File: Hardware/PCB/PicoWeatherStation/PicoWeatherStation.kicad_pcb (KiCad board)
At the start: 2 copper layers, 99.2 x 73 mm, 83 parts, among them J1 TOUCH_PANEL, J2 LCD_BL, Q1 AO3400A, SW1 SW_PICO_RST, SW2 SW_PICO_RST, SW3 SW_PICO_RST, SW4 SW_PICO_RST, SW5 SW_PICO_RST, SW6 SW_PICO_RST, SW7 SW_PICO_RST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

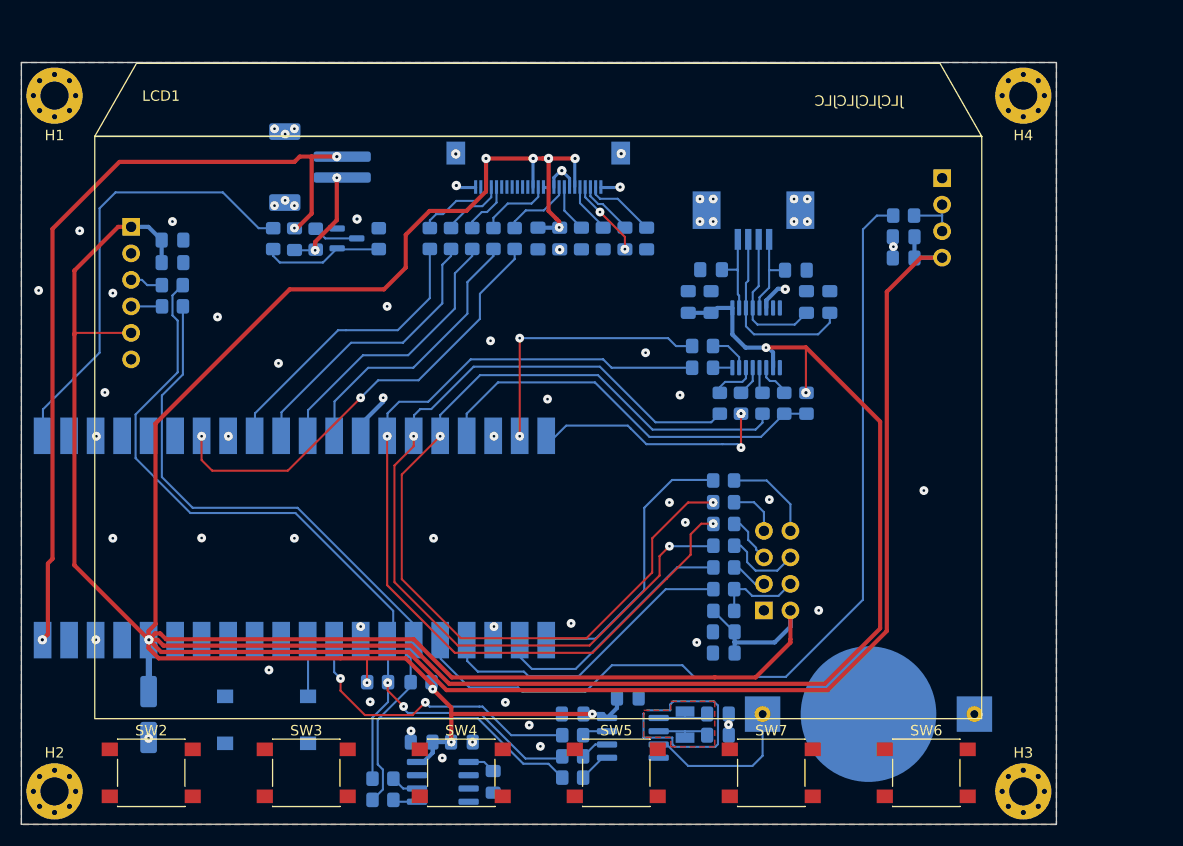
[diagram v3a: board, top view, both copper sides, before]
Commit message: PCB: wire-up the keyboard
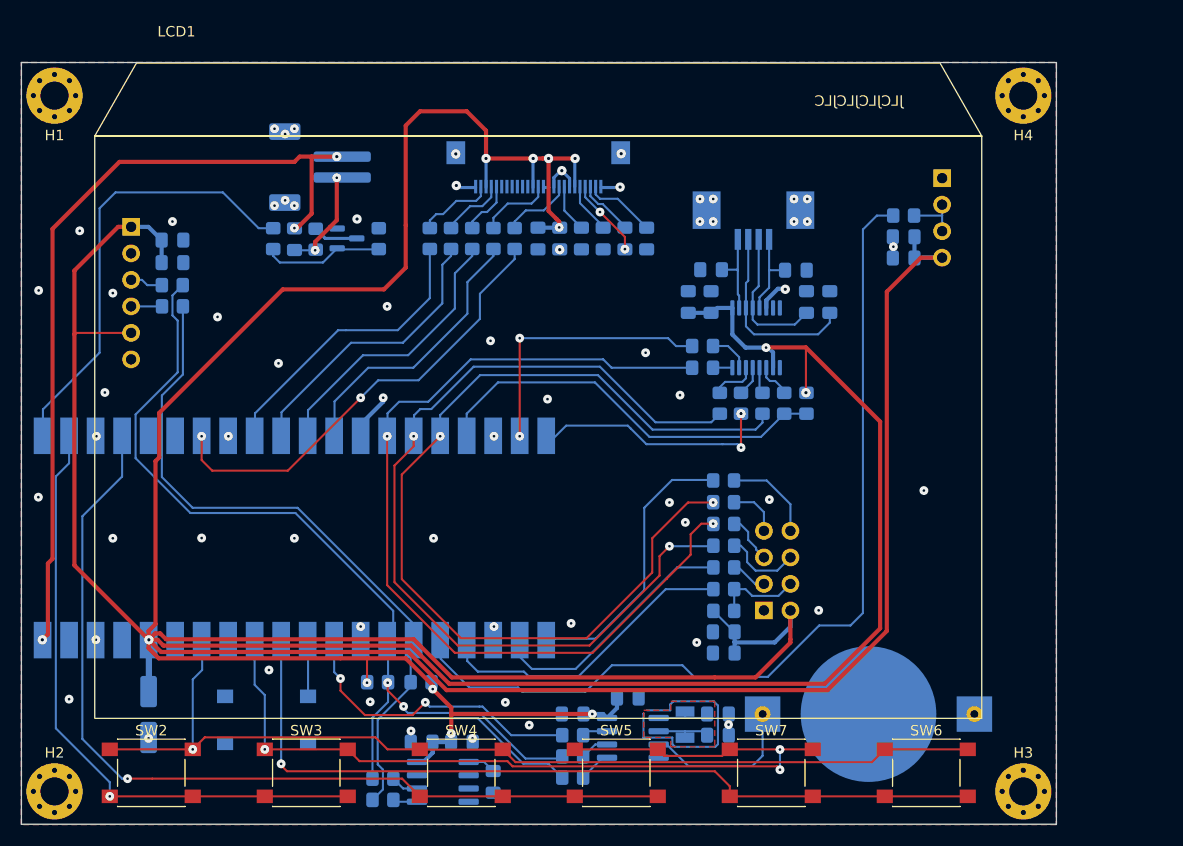
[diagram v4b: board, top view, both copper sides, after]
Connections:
- SW2 pad 1: unconnected-(SW2-Pad1) -> KBD_SCAN0
- SW2 pad 2: unconnected-(SW2-Pad2) -> KBD_DRV0
- SW3 pad 1: unconnected-(SW3-Pad1) -> KBD_SCAN1
- SW3 pad 2: unconnected-(SW3-Pad2) -> KBD_DRV0
- SW4 pad 1: unconnected-(SW4-Pad1) -> KBD_SCAN0
- SW4 pad 2: unconnected-(SW4-Pad2) -> KBD_DRV1
- SW5 pad 1: unconnected-(SW5-Pad1) -> KBD_SCAN1
- SW5 pad 2: unconnected-(SW5-Pad2) -> KBD_DRV1
- SW6 pad 1: unconnected-(SW6-Pad1) -> KBD_SCAN0
- SW6 pad 2: unconnected-(SW6-Pad2) -> KBD_DRV2
- SW7 pad 1: unconnected-(SW7-Pad1) -> KBD_SCAN1
- SW7 pad 2: unconnected-(SW7-Pad2) -> KBD_DRV2
- U1 pad 2: unconnected-(U1-Pad2) -> KBD_DRV0
- U1 pad 31: unconnected-(U1-Pad31) -> KBD_DRV2
- U1 pad 32: unconnected-(U1-Pad32) -> KBD_SCAN1
- U1 pad 34: unconnected-(U1-Pad34) -> KBD_SCAN0
- U1 pad 4: unconnected-(U1-Pad4) -> KBD_DRV1
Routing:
- net KBD_SCAN0: track 0.00 -> 96.0 mm, vias 0 -> 1
- net KBD_SCAN1: track 0.00 -> 87.2 mm, vias 0 -> 3
- net KBD_DRV1: track 0.00 -> 87.2 mm, vias 0 -> 1
- net KBD_DRV2: track 0.00 -> 80.5 mm, vias 0 -> 1
- net KBD_DRV0: track 0.00 -> 59.1 mm, vias 0 -> 1
- net VDD: track 542.2 -> 551.5 mm
- net ZR_OUT: track 88.0 -> 88.8 mm

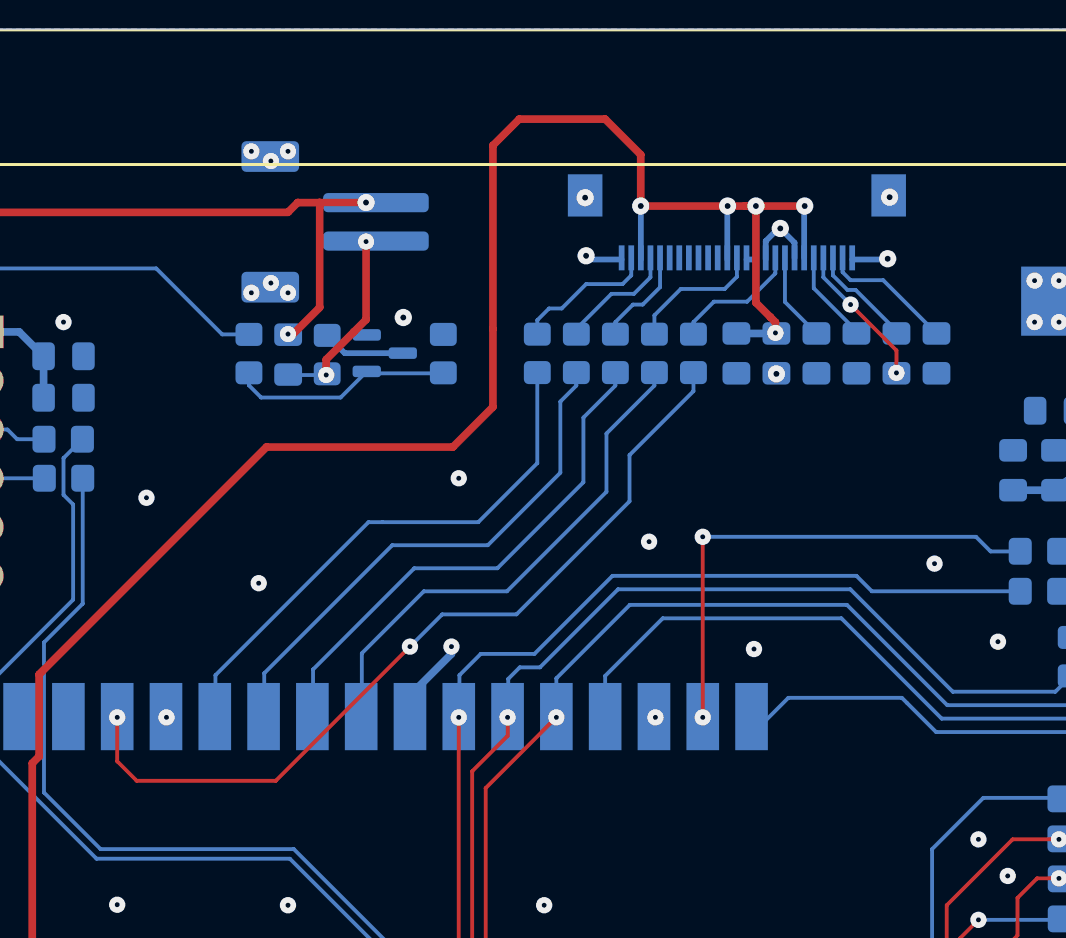
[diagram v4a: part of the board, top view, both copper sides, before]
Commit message: PCB: optimize high speed LCD signal tracks
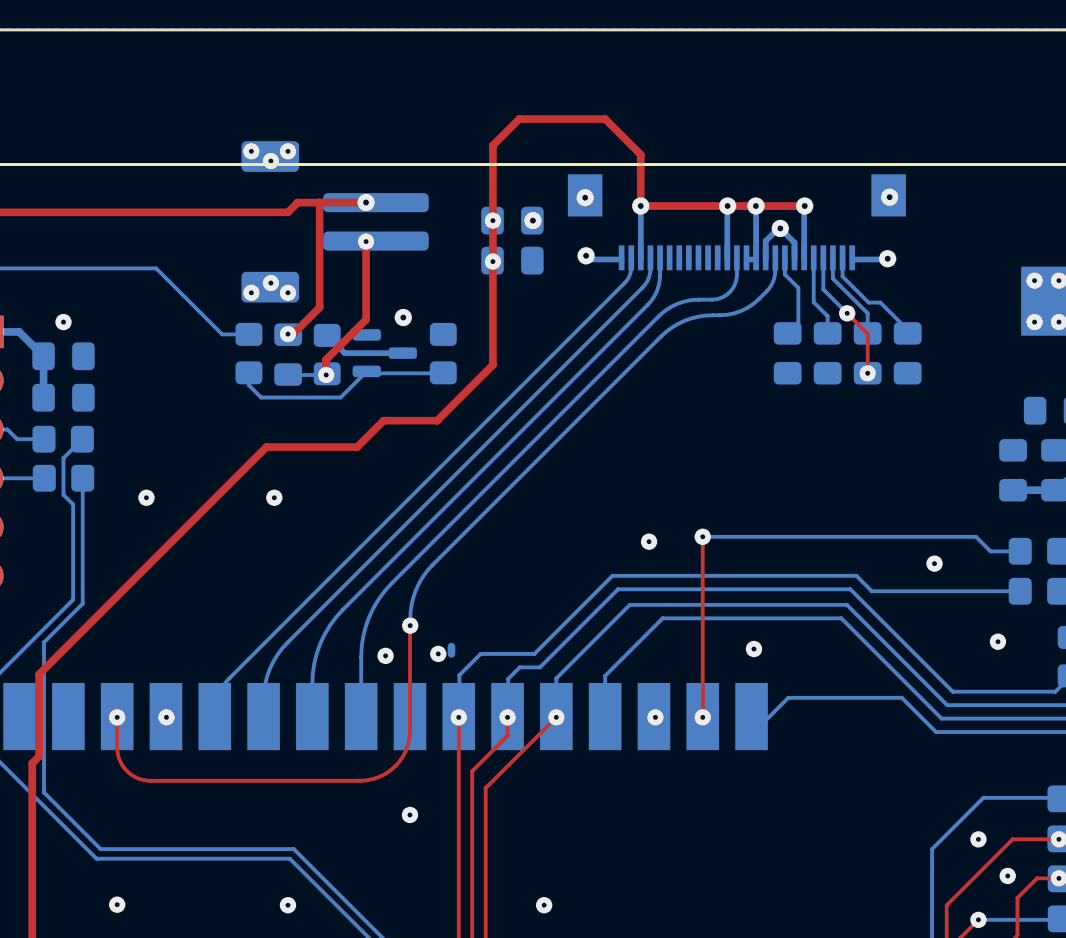
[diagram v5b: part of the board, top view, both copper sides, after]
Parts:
- removed R101, R102, R103, R104, R105: 270, Resistor_SMD:R_0805_2012Metric_Pad1.20x1.40mm_HandSolder
- moved C102 15.4 mm to (120.4, 49.3), turned to 0 degrees
- moved C101 12.6 mm to (120.4, 51.4), turned to 0 degrees
- moved C111 1.50 mm to (141.0, 56.2)
- moved C112 1.50 mm to (138.9, 56.2)
- moved C113 1.50 mm to (136.8, 56.2)
- moved C114 1.50 mm to (134.7, 56.2)
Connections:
- LCD1 pad 13: Net-(LCD1-Pad13) -> LCD_~{RST}
- LCD1 pad 21: Net-(LCD1-Pad21) -> LCD_D~{C}
- LCD1 pad 22: Net-(LCD1-Pad22) -> LCD_SDI
- LCD1 pad 24: Net-(LCD1-Pad24) -> LCD_SCK
- LCD1 pad 9: Net-(LCD1-Pad9) -> LCD_~{CS}
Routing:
- net VDD: track 551.5 -> 541.2 mm, vias 12 -> 13
- net LCD_~{CS}: track 43.5 -> 52.7 mm
- net Net-(LCD1-Pad24): track 7.48 -> 0.00 mm
- net Net-(LCD1-Pad13): track 7.08 -> 0.00 mm
- net Net-(LCD1-Pad9): track 6.74 -> 0.00 mm
- net Net-(LCD1-Pad22): track 6.24 -> 0.00 mm
- net LCD_~{RST}: track 27.7 -> 33.8 mm
- net Net-(LCD1-Pad21): track 5.22 -> 0.00 mm
- net LCD_SCK: track 29.1 -> 33.6 mm
- net LCD_SDI: track 28.5 -> 32.9 mm
- net LCD_D~{C}: track 27.9 -> 31.9 mm
- net GND: track 37.0 -> 34.0 mm, vias 63 -> 64
- net LCD_VG: track 6.94 -> 5.69 mm
- net LCD_XV0: track 5.54 -> 4.68 mm
- net LCD_VM: track 4.84 -> 4.23 mm
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
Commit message: PCB: do minor track optimization
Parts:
- moved C113 0.30 mm to (136.5, 56.2)
- moved C114 0.30 mm to (134.4, 56.2)
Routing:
- net VDD: track 541.2 -> 538.4 mm
- net GND: track 34.0 -> 33.6 mm, vias 64 -> 66
- net LCD_V0: vias 2 -> 0
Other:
- board text removed: "ZR_OUT"

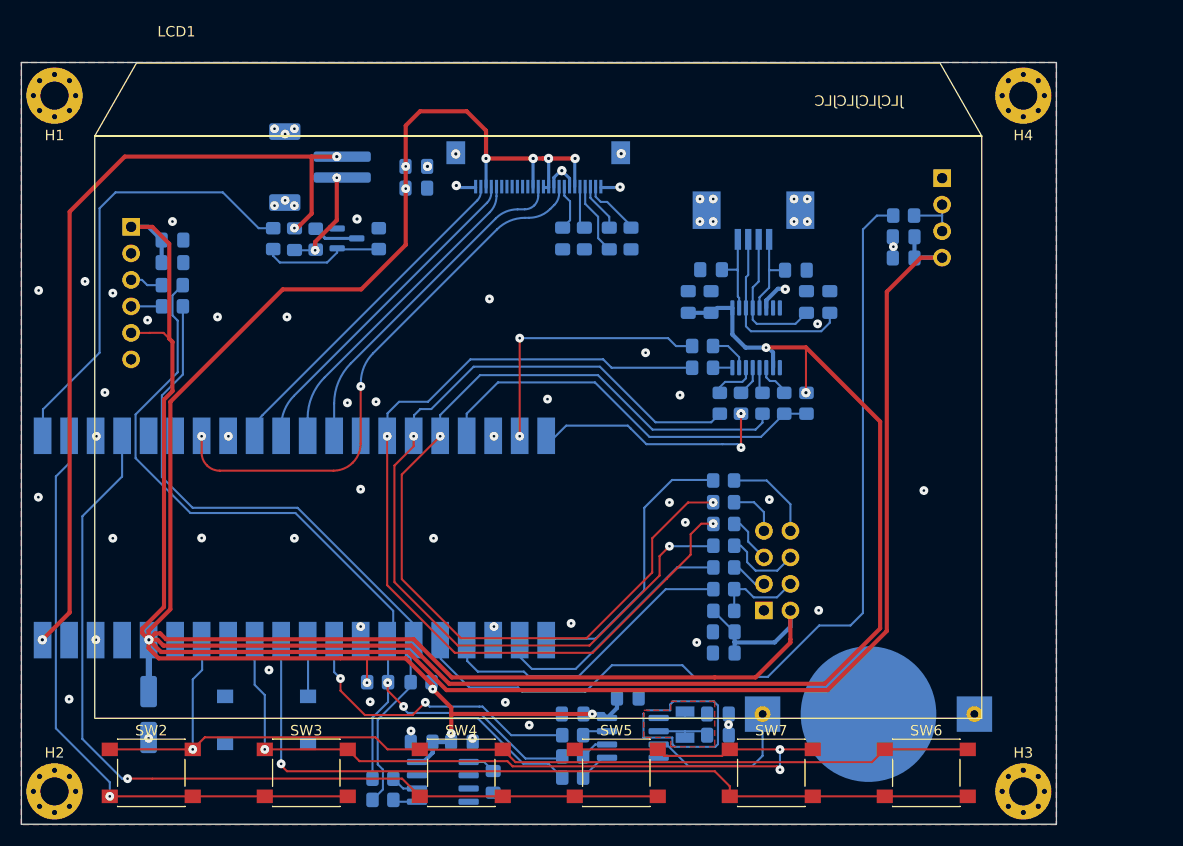
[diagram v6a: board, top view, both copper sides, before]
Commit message: PCB: optimize peripheral SPI signals
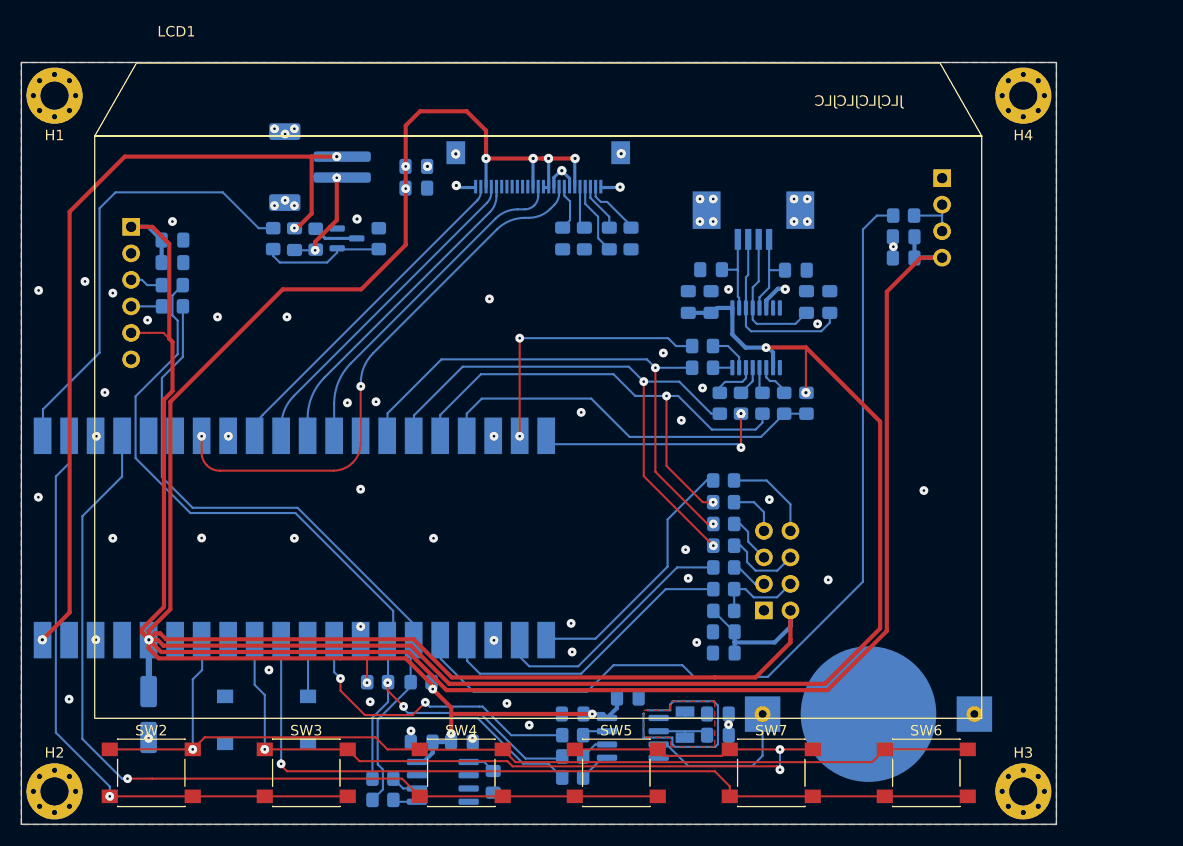
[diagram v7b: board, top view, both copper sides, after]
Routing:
- net SPI_PERI_MISO: track 93.4 -> 51.4 mm
- net SPI_PERI_SCK: track 89.2 -> 52.3 mm
- net SPI_PERI_MOSI: track 89.5 -> 54.5 mm
- net NRF_IRQ: track 29.2 -> 27.2 mm
- net ZR_OUT: track 88.8 -> 87.0 mm
- net TOUCH_BUSY: track 23.5 -> 22.1 mm
- net TOUCH_~{PENIRQ}: track 39.9 -> 38.6 mm
- net GND: vias 66 -> 69

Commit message: PCB: bigger footprint for the clock crystal
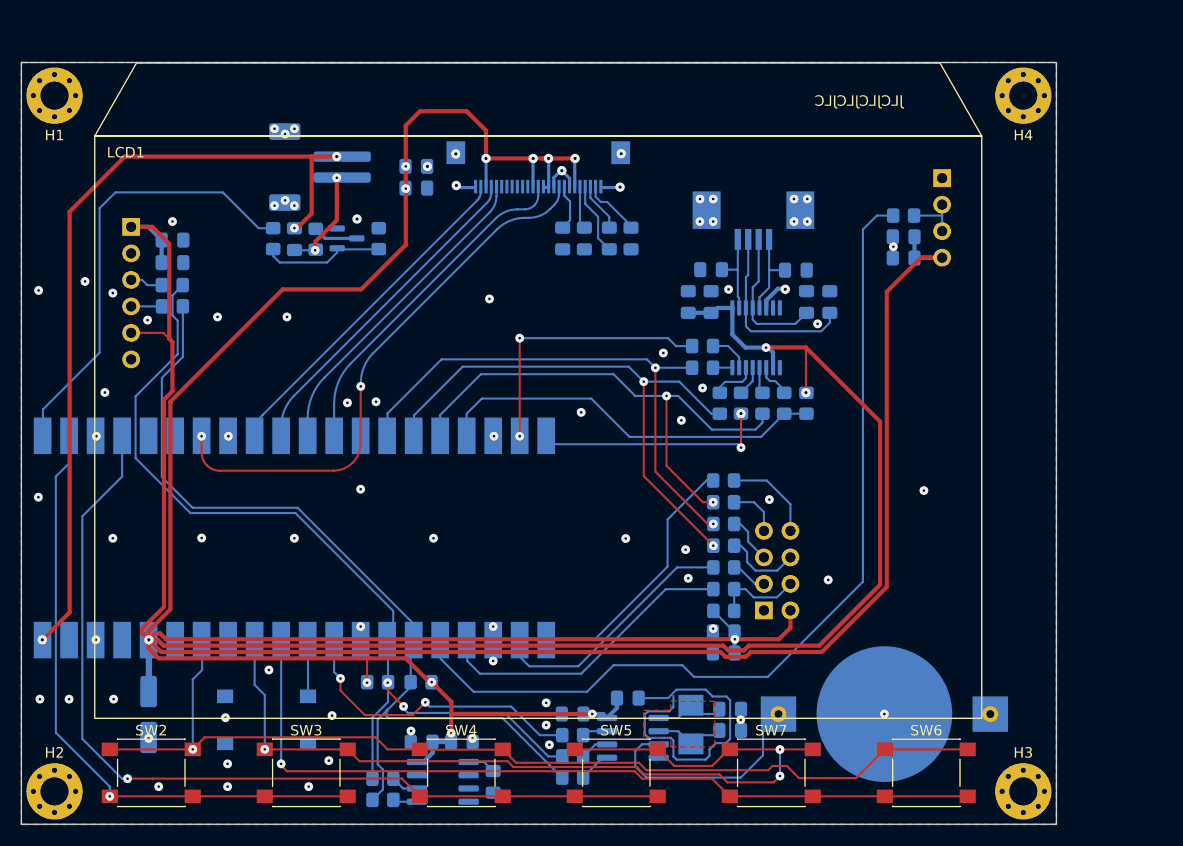
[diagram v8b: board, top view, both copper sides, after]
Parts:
- Y1: footprint Crystal:Crystal_SMD_3215-2Pin_3.2x1.5mm -> Crystal:Crystal_SMD_5032-2Pin_5.0x3.2mm
- moved BT1 1.52 mm to (165.2, 101.8)
- moved CX1 1.26 mm to (150.5, 101.3)
- moved CX2 1.26 mm to (150.5, 103.4)
- moved Y1 0.56 mm to (146.7, 102.8), turned to 90 degrees
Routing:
- net VDD: track 538.4 -> 517.5 mm, vias 13 -> 14
- net GND: track 33.6 -> 42.4 mm, vias 69 -> 79
- net Net-(BT1-Pad1): track 15.2 -> 23.3 mm
- net KBD_SCAN1: track 87.2 -> 89.4 mm
- net KBD_SCAN0: track 96.0 -> 97.6 mm
- net Net-(CX2-Pad1): track 5.43 -> 6.07 mm
- net Net-(CX1-Pad1): track 5.41 -> 6.05 mm
- net KBD_DRV2: track 80.5 -> 79.9 mm
